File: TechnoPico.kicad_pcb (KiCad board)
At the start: 2 copper layers, 138.3 x 70.6 mm, 171 parts, among them J1 USB_C_Receptacle_USB2.0, J2 Conn_01x02, J3 Conn_01x04, SW1 Test, SW2 Service, SW3 BOOTSEL, U1 RP2350_60QFN, U2 SN74LV1T34DBV, U3 XC6206PxxxMR, U4 USBLC6-2SC6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

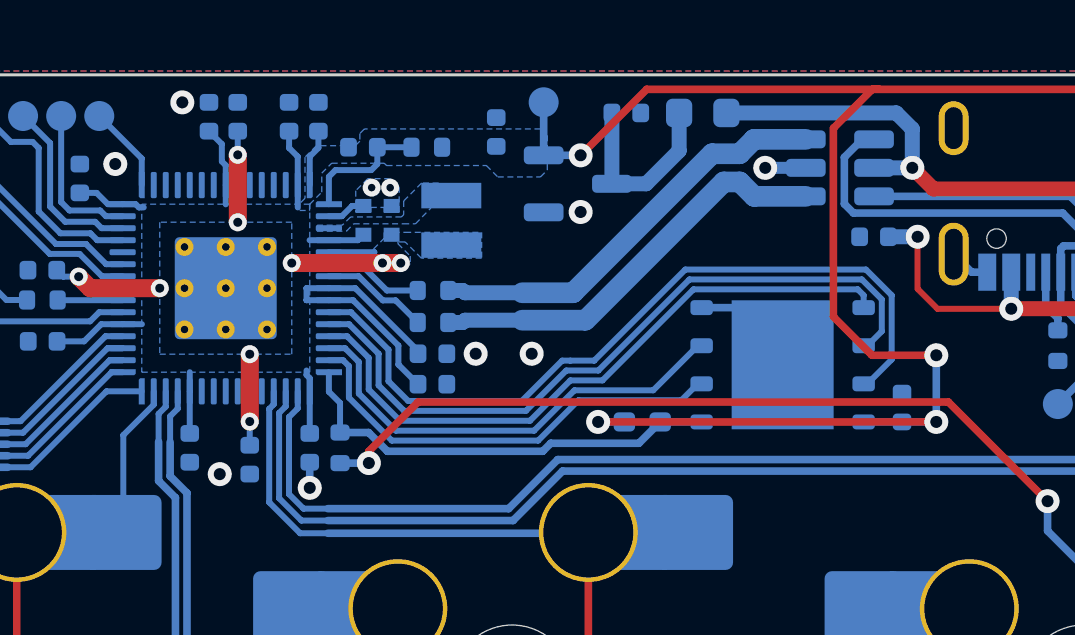
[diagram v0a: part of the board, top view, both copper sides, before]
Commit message: Routing changes, use custom RP2350 inductor, etc
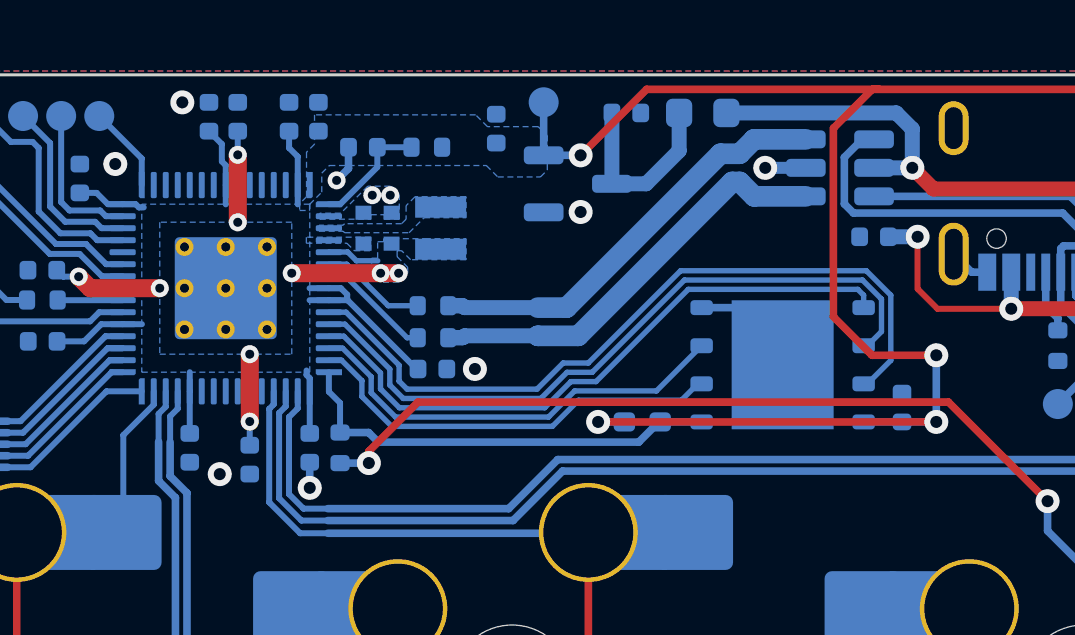
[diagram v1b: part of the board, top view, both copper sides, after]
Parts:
- removed C30: 100nF, Capacitor_SMD:C_0402_1005Metric
- C25, C26: footprint Capacitor_SMD:C_0402_1005Metric -> RP2350 Components:C_0402_1005Metric_small_pads
- L1: footprint PA4335.XXXNLT:PA4335.XXXNLT -> RP2350 Components:L_pol_2016
- moved C37 0.51 mm to (165.0, 60.6)
- moved R4 0.51 mm to (165.0, 58.5)
- moved R5 0.51 mm to (165.0, 59.6)
- moved L1 0.44 mm to (165.3, 55.9), turned to 90 degrees
- moved C25 0.26 mm to (162.7, 55.9)
- moved C26 0.26 mm to (163.7, 55.9)
- moved C20 0.11 mm to (167.2, 52.6)
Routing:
- net +3V3: track 89.8 -> 81.9 mm
- net USB_DP: track 14.0 -> 14.7 mm
- net QSPI_SD3: track 26.2 -> 25.5 mm
- net QSPI_SD1: track 14.9 -> 14.2 mm
- net QSPI_SD2: track 15.4 -> 14.7 mm
- net USB_DN: track 14.1 -> 14.7 mm
- net QSPI_SCLK: track 24.2 -> 23.5 mm
- net QSPI_SD0: track 21.9 -> 21.3 mm
